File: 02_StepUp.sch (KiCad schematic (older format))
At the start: 1 part

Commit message: 3v3 über LDO von BMS enablen. Bluetooth hinzugefügt
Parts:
- removed J?: Conn_01x02_Female, symbol Connector:Conn_01x02_Female
- added C301: 1000u35V, symbol Device:CP_Small
- added C302: 1n2, symbol Device:C_Small
- added C303: 100n, symbol Device:C_Small
- added C304: 25uF, symbol Device:C_Small
- added C305: 1000u60V, symbol Device:CP_Small
- added D301: STPS2045C, symbol Device:D_Schottky_Small
- added L301: 10uH, symbol Device:L_Small
- added Q301: Q_NPN_BCE, symbol Device:Q_NPN_BCE
- added Q302: STP75NF75, symbol Device:Q_NMOS_DGS
- added R301: 5K1, symbol Device:R_Small
- added R302: 15K, symbol Device:R_Small
- added R303: 30K, symbol Device:R_Small
- added R304: 100K, symbol Device:R_Small
- added R305, R309: 1K, symbol Device:R_Small
- added R306: R010, symbol Device:R_Small
- added R307: 10K, symbol Device:R_Variable
- added R308: 2K94, symbol Device:R_Small
- added U301: L7812, symbol Regulator_Linear:L7812
- added U302: UC3843_SOIC8, Package_SO:SOIC-8_3.9x4.9mm_P1.27mm, symbol Regulator_Controller:UC3843_SOIC8
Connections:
- net labels added: FB_BOOST, GNDPWR, PACK+, POWER_32V
- wire segments 0 -> 59
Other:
- note added: "UC1842 Step Up von aliexpress yo\n\n"

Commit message: Footprintzuordnung angefangen
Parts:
- added C306: C_Small, Capacitor_SMD:C_0603_1608Metric_Pad1.05x0.95mm_HandSolder, symbol Device:C_Small
- C301: value 1000u35V -> 1000u35V EEV-FK1V102V; footprint (none) -> Capacitor_SMD:CP_Elec_16x17.5
- C302, C303: footprint (none) -> Capacitor_SMD:C_0603_1608Metric_Pad1.05x0.95mm_HandSolder
- C304: footprint (none) -> Capacitor_SMD:CP_Elec_5x5.4
- C305: value 1000u60V -> 1000u60V EEV-FK1V102V; footprint (none) -> Capacitor_SMD:CP_Elec_16x17.5
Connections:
- net labels added: POWER_AMP, SYSTEM_LOAD
- net labels removed: PACK+, POWER_32V
- wire segments 59 -> 60
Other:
- note added: "Close to VREF Pin"
- moved on the sheet: C303
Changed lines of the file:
@@
 P 7400 3600
 F 0 "C305" H 7488 3646 50  0000 L CNN
-F 1 "1000u60V" H 7488 3555 50  0000 L CNN
-F 2 "" H 7400 3600 50  0001 C CNN
+F 1 "1000u60V EEV-FK1V102V " H 6800 3500 50  0000 L CNN
+F 2 "Capacitor_SMD:CP_Elec_16x17.5" H 7400 3600 50  0001 C CNN
 F 3 "~" H 7400 3600 50  0001 C CNN
 	1    7400 3600
@@
 L Device:C_Small C303
 U 1 1 5E79837A
-P 4400 3850
-F 0 "C303" H 4492 3896 50  0000 L CNN
-F 1 "100n" H 4492 3805 50  0000 L CNN
-F 2 "" H 4400 3850 50  0001 C CNN
-F 3 "~" H 4400 3850 50  0001 C CNN
-	1    4400 3850
-	1    0    0    -1
-$EndComp
-Wire Wire Line
-	4750 3650 4400 3650
-Wire Wire Line
-	4400 3650 4400 3750
+P 4600 3850
+F 0 "C303" H 4400 3950 50  0000 L CNN
+F 1 "100n" H 4400 3750 50  0000 L CNN
+F 2 "Capacitor_SMD:C_0603_1608Metric_Pad1.05x0.95mm_HandSolder" H 4600 3850 50  0001 C CNN
+F 3 "~" H 4600 3850 50  0001 C CNN
+	1    4600 3850
+	1    0    0    -1
+$EndComp
+Wire Wire Line
+	4750 3650 4600 3650
+Wire Wire Line
+	4600 3650 4600 3750
 Wire Wire Line
 	7900 3900 8250 3900
@@
 FB_BOOST
 Wire Wire Line
-	4400 3950 4400 4150
-Wire Wire Line
-	4400 4150 4650 4150
-Wire Wire Line
-	4750 3800 4650 3800
-Wire Wire Line
-	4650 3800 4650 4150
-Connection ~ 4650 4150
-Wire Wire Line
-	4650 4150 4800 4150
+	4600 3950 4600 4150
+Wire Wire Line
+	4600 4150 4750 4150
+Wire Wire Line
+	4750 3800 4750 4150
+Connection ~ 4750 4150
+Wire Wire Line
+	4750 4150 4800 4150
 $Comp
 L power:GNDPWR #PWR0123
@@
 F 0 "C302" H 4092 3896 50  0000 L CNN
 F 1 "1n2" H 4092 3805 50  0000 L CNN
-F 2 "" H 4000 3850 50  0001 C CNN
+F 2 "Capacitor_SMD:C_0603_1608Metric_Pad1.05x0.95mm_HandSolder" H 4000 3850 50  0001 C CNN
 F 3 "~" H 4000 3850 50  0001 C CNN
 	1    4000 3850
@@
 	4000 4200 4000 3950
 Wire Wire Line
-	4750 3500 4750 3600
-Wire Wire Line
-	4750 3600 4200 3600
-Wire Wire Line
-	4200 3600 4200 3700
-Wire Wire Line
-	4200 3700 4000 3700
+	4450 3700 4000 3700
 Connection ~ 4000 3700
 Wire Wire Line
@@
 Connection ~ 6050 2600
 Text GLabel 3900 2600 0    50   Input ~ 0
-PACK+
+SYSTEM_LOAD
 $Comp
 L Regulator_Linear:L7812 U301
@@
 P 3950 3000
 F 0 "C301" H 4038 3046 50  0000 L CNN
-F 1 "1000u35V" H 4038 2955 50  0000 L CNN
-F 2 "" H 3950 3000 50  0001 C CNN
+F 1 "1000u35V EEV-FK1V102V " H 3400 2900 50  0000 L CNN
+F 2 "Capacitor_SMD:CP_Elec_16x17.5" H 3950 3000 50  0001 C CNN
 F 3 "~" H 3950 3000 50  0001 C CNN
 	1    3950 3000
@@
 F 0 "C304" H 4992 3046 50  0000 L CNN
 F 1 "25uF" H 4992 2955 50  0000 L CNN
-F 2 "" H 4900 3000 50  0001 C CNN
+F 2 "Capacitor_SMD:CP_Elec_5x5.4" H 4900 3000 50  0001 C CNN
 F 3 "~" H 4900 3000 50  0001 C CNN
 	1    4900 3000
@@
 	5900 4200 5900 3700
 Text GLabel 8250 3150 2    50   Output ~ 0
-POWER_32V
+POWER_AMP
+$Comp
+L Device:C_Small C306
+U 1 1 5EB77D85
+P 2800 3850
+F 0 "C306" H 2892 3896 50  0000 L CNN
+F 1 "C_Small" H 2892 3805 50  0000 L CNN
+F 2 "Capacitor_SMD:C_0603_1608Metric_Pad1.05x0.95mm_HandSolder" H 2800 3850 50  0001 C CNN
+F 3 "~" H 2800 3850 50  0001 C CNN
+	1    2800 3850
+	1    0    0    -1
+$EndComp
+Wire Wire Line
+	4750 3500 4450 3500
+Wire Wire Line
+	4450 3500 4450 3700
+Wire Wire Line
+	3600 3400 2800 3400
+Wire Wire Line
+	2800 3400 2800 3750
+Connection ~ 3600 3400
+$Comp
+L power:GNDPWR #PWR0178
+U 1 1 5EB800AE
+P 2800 4100
+F 0 "#PWR0178" H 2800 3900 50  0001 C CNN
+F 1 "GNDPWR" H 2804 3946 50  0000 C CNN
+F 2 "" H 2800 4050 50  0001 C CNN
+F 3 "" H 2800 4050 50  0001 C CNN
+	1    2800 4100
+	1    0    0    -1
+$EndComp
+Wire Wire Line
+	2800 3950 2800 4100
+Text Notes 2700 4100 1    50   ~ 0
+Close to VREF Pin
+$Comp
+L power:PWR_FLAG #FLG0110
+U 1 1 5EBB228F
+P 7900 3150
+F 0 "#FLG0110" H 7900 3225 50  0001 C CNN
+F 1 "PWR_FLAG" H 7900 3324 50  0000 C CNN
+F 2 "" H 7900 3150 50  0001 C CNN
+F 3 "~" H 7900 3150 50  0001 C CNN
+	1    7900 3150
+	1    0    0    -1
+$EndComp
 $EndSCHEMATC

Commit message: fast alle footprints herausgesucht. Spulen typen rausgesucht: Bourns spulen
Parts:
- removed D301: STPS2045C, symbol Device:D_Schottky_Small
- removed Q301: Q_NPN_BCE, symbol Device:Q_NPN_BCE
- removed Q302: STP75NF75, symbol Device:Q_NMOS_DGS
- removed R307: 10K, symbol Device:R_Variable
- added D301: STPS2045C, Package_TO_SOT_SMD:TO-263-2, symbol Device:D_Schottky_x2_KCom_AKA
- added HS301, HS302: Heatsink_Pad, Heatsink:Heatsink_AAVID_573300D00010G_TO-263, symbol Mechanical:Heatsink_Pad
- added Q301: MMBT2222LT1G, Package_TO_SOT_SMD:SOT-23, symbol Device:Q_NPN_BEC
- added Q302: TK7R7P10PL, Package_TO_SOT_SMD:TO-263-2, symbol Device:Q_NMOS_GDS
- added RV301: 10K, Potentiometer_SMD:Potentiometer_Bourns_3314J_Vertical, symbol Device:R_POT
- L301: value 10uH -> 10uH PQ2617BHA-100K; footprint (none) -> Inductor_SMD:PQ2617BHA-330K
- R301, R302, R303, R304, R305, R308, R309: footprint (none) -> Resistor_SMD:R_0603_1608Metric_Pad1.05x0.95mm_HandSolder
- R306: footprint (none) -> Resistor_SMD:R_1206_3216Metric_Pad1.42x1.75mm_HandSolder
- U301: footprint (none) -> Package_TO_SOT_SMD:TO-263-2
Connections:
- wire segments 60 -> 74
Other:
- note added: "STB75NF75"
- note added: "UC1842 Step Up von aliexpress yo\nhttps://www.360customs.de/2014/05/103050100w-led-applikation-treiber/?cookie-state-change=1586628857397\n"
- note removed: "UC1842 Step Up von aliexpress yo\n\n"
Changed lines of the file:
@@
 $EndDescr
 Text Notes 5000 1550 0    50   ~ 0
-UC1842 Step Up von aliexpress yo\n\n
+UC1842 Step Up von aliexpress yo\nhttps://www.360customs.de/2014/05/103050100w-led-applikation-treiber/?cookie-state-change=1586628857397\n
 $Comp
 L Regulator_Controller:UC3843_SOIC8 U302
@@
 F 0 "R303" H 5959 3646 50  0000 L CNN
 F 1 "30K" H 5959 3555 50  0000 L CNN
-F 2 "" H 5900 3600 50  0001 C CNN
+F 2 "Resistor_SMD:R_0603_1608Metric_Pad1.05x0.95mm_HandSolder" H 5900 3600 50  0001 C CNN
 F 3 "~" H 5900 3600 50  0001 C CNN
 	1    5900 3600
@@
 F 0 "R305" V 6104 3800 50  0000 C CNN
 F 1 "1K" V 6195 3800 50  0000 C CNN
-F 2 "" H 6300 3800 50  0001 C CNN
+F 2 "Resistor_SMD:R_0603_1608Metric_Pad1.05x0.95mm_HandSolder" H 6300 3800 50  0001 C CNN
 F 3 "~" H 6300 3800 50  0001 C CNN
 	1    6300 3800
@@
 F 0 "R306" H 6491 4054 50  0000 R CNN
 F 1 "R010" H 6491 4145 50  0000 R CNN
-F 2 "" H 6550 4100 50  0001 C CNN
+F 2 "Resistor_SMD:R_1206_3216Metric_Pad1.42x1.75mm_HandSolder" H 6550 4100 50  0001 C CNN
 F 3 "~" H 6550 4100 50  0001 C CNN
 	1    6550 4100
 	-1   0    0    1
-$EndComp
-$Comp
-L Device:Q_NMOS_DGS Q302
-U 1 1 5E7966A0
-P 6450 3400
-F 0 "Q302" H 6656 3446 50  0000 L CNN
-F 1 "STP75NF75" H 6656 3355 50  0000 L CNN
-F 2 "" H 6650 3500 50  0001 C CNN
-F 3 "~" H 6450 3400 50  0001 C CNN
-	1    6450 3400
-	1    0    0    -1
 $EndComp
 $Comp
@@
 F 0 "R304" H 5991 2854 50  0000 R CNN
 F 1 "100K" H 5991 2945 50  0000 R CNN
-F 2 "" H 6050 2900 50  0001 C CNN
+F 2 "Resistor_SMD:R_0603_1608Metric_Pad1.05x0.95mm_HandSolder" H 6050 2900 50  0001 C CNN
 F 3 "~" H 6050 2900 50  0001 C CNN
 	1    6050 2900
@@
 P 6550 2900
 F 0 "L301" H 6598 2946 50  0000 L CNN
-F 1 "10uH" H 6598 2855 50  0000 L CNN
-F 2 "" H 6550 2900 50  0001 C CNN
-F 3 "~" H 6550 2900 50  0001 C CNN
+F 1 "10uH PQ2617BHA-100K " H 6598 2855 50  0000 L CNN
+F 2 "Inductor_SMD:PQ2617BHA-330K" H 6550 2900 50  0001 C CNN
+F 3 "https://www.mouser.de/datasheet/2/54/bourns_PQ2617BHA_datasheet-1159314.pdf" H 6550 2900 50  0001 C CNN
 	1    6550 2900
 	1    0    0    -1
@@
 Wire Wire Line
 	6550 3000 6550 3150
-$Comp
-L Device:D_Schottky_Small D301
-U 1 1 5E796C90
-P 7250 3150
-F 0 "D301" H 7250 2945 50  0000 C CNN
-F 1 "STPS2045C" H 7250 3036 50  0000 C CNN
-F 2 "" V 7250 3150 50  0001 C CNN
-F 3 "~" V 7250 3150 50  0001 C CNN
-	1    7250 3150
-	-1   0    0    1
-$EndComp
-Wire Wire Line
-	7150 3150 6550 3150
 Connection ~ 6550 3150
 Wire Wire Line
@@
 	7400 4200 7400 3700
 $Comp
-L Device:R_Variable R307
-U 1 1 5E79725B
-P 7900 3400
-F 0 "R307" H 8028 3446 50  0000 L CNN
-F 1 "10K" H 8028 3355 50  0000 L CNN
-F 2 "" V 7830 3400 50  0001 C CNN
-F 3 "~" H 7900 3400 50  0001 C CNN
-	1    7900 3400
-	1    0    0    -1
-$EndComp
-$Comp
 L Device:R_Small R308
 U 1 1 5E7975A3
@@
 F 0 "R308" H 7841 3704 50  0000 R CNN
 F 1 "2K94" H 7841 3795 50  0000 R CNN
-F 2 "" H 7900 3750 50  0001 C CNN
+F 2 "Resistor_SMD:R_0603_1608Metric_Pad1.05x0.95mm_HandSolder" H 7900 3750 50  0001 C CNN
 F 3 "~" H 7900 3750 50  0001 C CNN
 	1    7900 3750
@@
 F 0 "R309" H 7841 4004 50  0000 R CNN
 F 1 "1K" H 7841 4095 50  0000 R CNN
-F 2 "" H 7900 4050 50  0001 C CNN
+F 2 "Resistor_SMD:R_0603_1608Metric_Pad1.05x0.95mm_HandSolder" H 7900 4050 50  0001 C CNN
 F 3 "~" H 7900 4050 50  0001 C CNN
 	1    7900 4050
@@
 	7900 3950 7900 3900
 Wire Wire Line
-	7900 3650 7900 3550
+	7900 3650 7900 3600
 $Comp
 L power:GNDPWR #PWR0122
@@
 	7900 3250 7900 3150
 Wire Wire Line
-	7900 3150 7400 3150
+	7900 3150 7600 3150
 Connection ~ 7400 3150
 Wire Wire Line
@@
 Wire Wire Line
 	4600 3650 4600 3750
-Wire Wire Line
-	7900 3900 8250 3900
 Connection ~ 7900 3900
 Wire Wire Line
 	7900 3900 7900 3850
-Text Label 8250 3900 0    50   ~ 0
-FB_BOOST
-Text Label 4800 4150 0    50   ~ 0
+Text Label 6500 4600 0    50   ~ 0
 FB_BOOST
 Wire Wire Line
@@
 	4750 3800 4750 4150
 Connection ~ 4750 4150
-Wire Wire Line
-	4750 4150 4800 4150
 $Comp
 L power:GNDPWR #PWR0123
@@
 F 0 "R302" H 4059 3546 50  0000 L CNN
 F 1 "15K" H 4059 3455 50  0000 L CNN
-F 2 "" H 4000 3500 50  0001 C CNN
+F 2 "Resistor_SMD:R_0603_1608Metric_Pad1.05x0.95mm_HandSolder" H 4000 3500 50  0001 C CNN
 F 3 "~" H 4000 3500 50  0001 C CNN
 	1    4000 3500
@@
 Wire Wire Line
 	4000 3700 4000 3750
-$Comp
-L Device:Q_NPN_BCE Q301
-U 1 1 5E79D498
-P 3700 3700
-F 0 "Q301" H 3890 3746 50  0000 L CNN
-F 1 "Q_NPN_BCE" H 3890 3655 50  0000 L CNN
-F 2 "" H 3900 3800 50  0001 C CNN
-F 3 "~" H 3700 3700 50  0001 C CNN
-	1    3700 3700
-	-1   0    0    -1
-$EndComp
 Wire Wire Line
 	4000 3700 3900 3700
@@
 F 0 "R301" H 3659 4146 50  0000 L CNN
 F 1 "5K1" H 3659 4055 50  0000 L CNN
-F 2 "" H 3600 4100 50  0001 C CNN
+F 2 "Resistor_SMD:R_0603_1608Metric_Pad1.05x0.95mm_HandSolder" H 3600 4100 50  0001 C CNN
 F 3 "~" H 3600 4100 50  0001 C CNN
 	1    3600 4100
@@
 F 0 "U301" H 4550 3042 50  0000 C CNN
 F 1 "L7812" H 4550 2951 50  0000 C CNN
-F 2 "" H 4575 2650 50  0001 L CIN
+F 2 "Package_TO_SOT_SMD:TO-263-2" H 4575 2650 50  0001 L CIN
 F 3 "http://www.st.com/content/ccc/resource/technical/document/datasheet/41/4f/b3/b0/12/d4/47/88/CD00000444.pdf/files/CD00000444.pdf/jcr:content/translations/en.CD00000444.pdf" H 4550 2750 50  0001 C CNN
 	1    4550 2800
@@
 	1    0    0    -1
 $EndComp
+$Comp
+L Mechanical:Heatsink_Pad HS301
+U 1 1 5EC9B13F
+P 7600 2700
+F 0 "HS301" H 7741 2741 50  0000 L CNN
+F 1 "Heatsink_Pad" H 7741 2650 50  0000 L CNN
+F 2 "Heatsink:Heatsink_AAVID_573300D00010G_TO-263" H 7612 2650 50  0001 C CNN
+F 3 "~" H 7612 2650 50  0001 C CNN
+	1    7600 2700
+	1    0    0    -1
+$EndComp
+Wire Wire Line
+	7600 2800 7600 3150
+Connection ~ 7600 3150
+Wire Wire Line
+	7600 3150 7400 3150
+$Comp
+L Device:Q_NMOS_GDS Q302
+U 1 1 5E929C35
+P 6450 3400
+F 0 "Q302" H 6750 3400 50  0000 L CNN
+F 1 "TK7R7P10PL" V 6700 3150 50  0000 L CNN
+F 2 "Package_TO_SOT_SMD:TO-263-2" H 6650 3500 50  0001 C CNN
+F 3 "https://www.mouser.de/datasheet/2/408/TK7R7P10PL_datasheet_en_20180219-1568652.pdf" H 6450 3400 50  0001 C CNN
+	1    6450 3400
+	1    0    0    -1
+$EndComp
+$Comp
+L Mechanical:Heatsink_Pad HS302
+U 1 1 5E929E76
+P 6400 2450
+F 0 "HS302" H 6541 2491 50  0000 L CNN
+F 1 "Heatsink_Pad" H 6541 2400 50  0000 L CNN
+F 2 "Heatsink:Heatsink_AAVID_573300D00010G_TO-263" H 6412 2400 50  0001 C CNN
+F 3 "~" H 6412 2400 50  0001 C CNN
+	1    6400 2450
+	1    0    0    -1
+$EndComp
+Wire Wire Line
+	6400 2550 6400 3150
+Wire Wire Line
+	6400 3150 6550 3150
+Text Notes 6750 3600 0    50   ~ 0
+STB75NF75
+$Comp
+L Device:D_Schottky_x2_KCom_AKA D301
+U 1 1 5EED4F08
+P 7150 3150
+F 0 "D301" V 7650 3050 50  0000 L CNN
+F 1 "STPS2045C" V 7550 3000 50  0000 L CNN
+F 2 "Package_TO_SOT_SMD:TO-263-2" H 7150 3150 50  0001 C CNN
+F 3 "https://www.mouser.de/datasheet/2/389/cd00268203-1797199.pdf" H 7150 3150 50  0001 C CNN
+	1    7150 3150
+	0    -1   -1   0
+$EndComp
+Wire Wire Line
+	7150 3450 7050 3450
+Wire Wire Line
+	7050 3450 7050 3150
+Wire Wire Line
+	7050 2850 7150 2850
+Wire Wire Line
+	6550 3150 7050 3150
+Connection ~ 7050 3150
+Wire Wire Line
+	7050 3150 7050 2850
+Wire Wire Line
+	4750 4150 4750 4600
+Wire Wire Line
+	4750 4600 7650 4600
+Wire Wire Line
+	7650 4600 7650 3900
+Wire Wire Line
+	7650 3900 7900 3900
+$Comp
+L Device:Q_NPN_BEC Q301
+U 1 1 5EEE6C27
+P 3700 3700
+F 0 "Q301" H 3890 3746 50  0000 L CNN
+F 1 "MMBT2222LT1G" H 3890 3655 50  0000 L CNN
+F 2 "Package_TO_SOT_SMD:SOT-23" H 3900 3800 50  0001 C CNN
+F 3 "https://www.mouser.de/datasheet/2/308/MMBT2222LT1-D-1811600.pdf" H 3700 3700 50  0001 C CNN
+	1    3700 3700
+	-1   0    0    -1
+$EndComp
+$Comp
+L Device:R_POT RV301
+U 1 1 5EEEB2DA
+P 7900 3400
+F 0 "RV301" H 7830 3446 50  0000 R CNN
+F 1 "10K" H 7830 3355 50  0000 R CNN
+F 2 "Potentiometer_SMD:Potentiometer_Bourns_3314J_Vertical" H 7900 3400 50  0001 C CNN
+F 3 "https://www.mouser.de/datasheet/2/54/tc33-778219.pdf" H 7900 3400 50  0001 C CNN
+	1    7900 3400
+	1    0    0    -1
+$EndComp
+Wire Wire Line
+	8050 3400 8100 3400
+Wire Wire Line
+	8100 3400 8100 3600
+Wire Wire Line
+	8100 3600 7900 3600
+Connection ~ 7900 3600
+Wire Wire Line
+	7900 3600 7900 3550
 $EndSCHEMATC

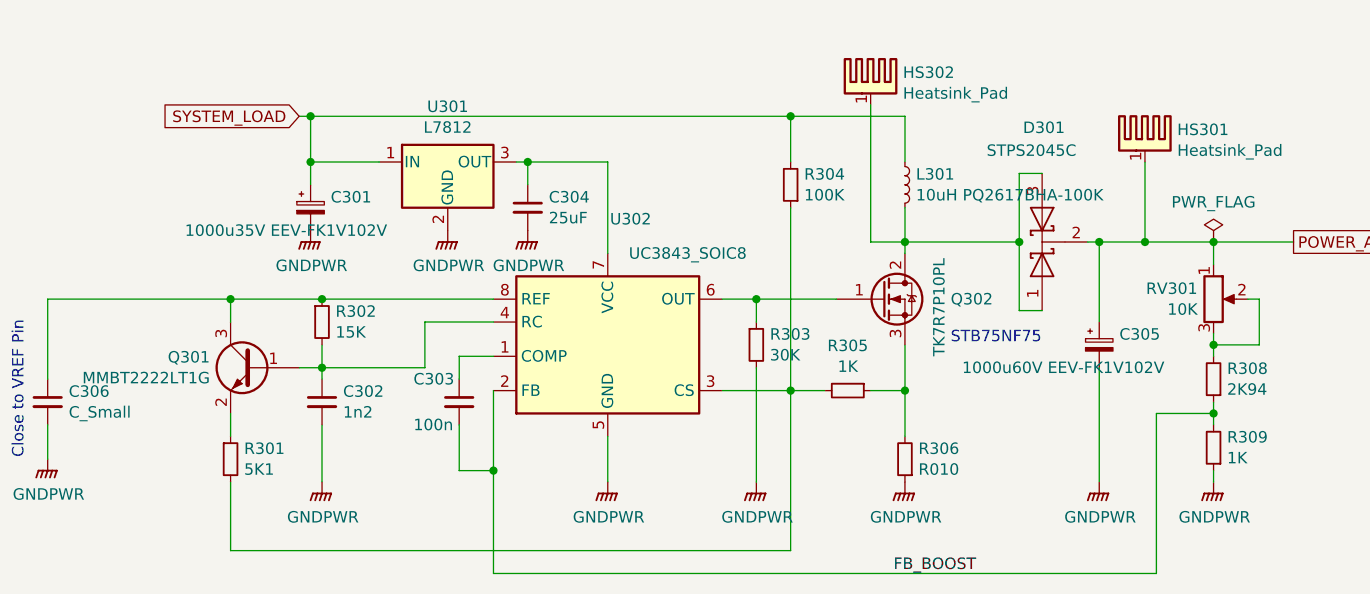
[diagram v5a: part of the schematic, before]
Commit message: Alle Parts geplaced: Dimension der Platine 200x105qmm. TODO Anzeige überarbeiten
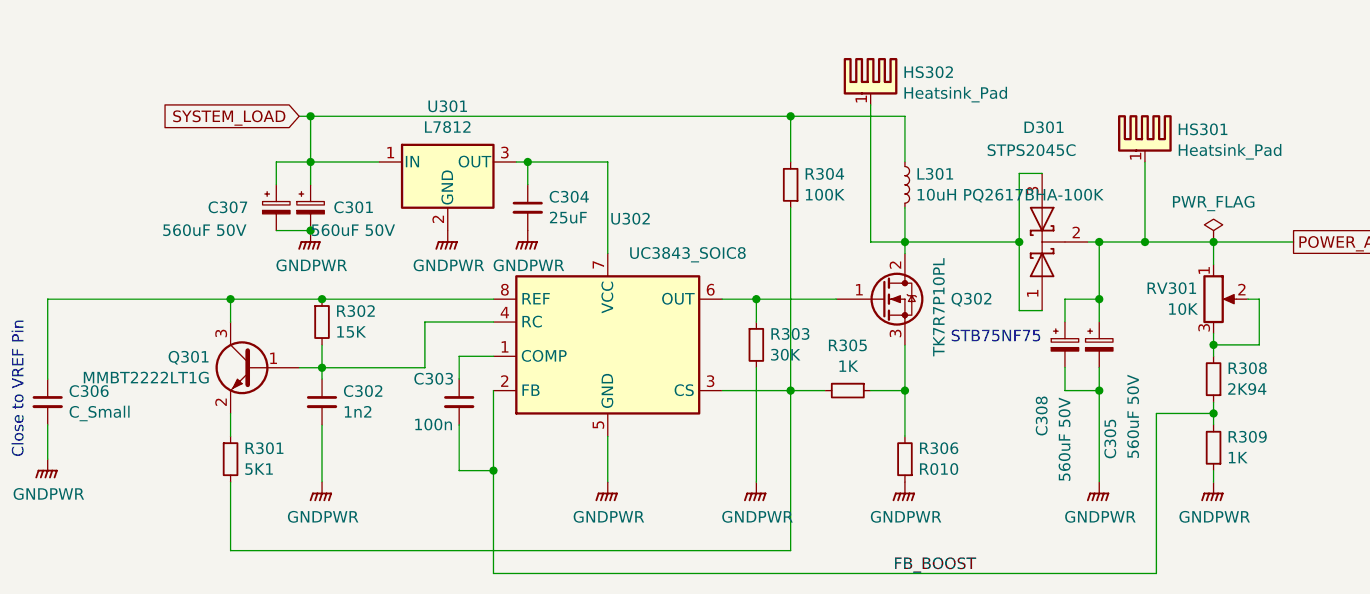
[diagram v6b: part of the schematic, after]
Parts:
- added C307, C308: 560uF 50V, Capacitor_THT:CP_Radial_D12.5mm_P5.00mm, symbol Device:CP_Small
- C301: value 1000u35V EEV-FK1V102V -> 560uF 50V; footprint Capacitor_SMD:CP_Elec_16x17.5 -> Capacitor_THT:CP_Radial_D12.5mm_P5.00mm
- C305: value 1000u60V EEV-FK1V102V -> 560uF 50V; footprint Capacitor_SMD:CP_Elec_16x17.5 -> Capacitor_THT:CP_Radial_D12.5mm_P5.00mm
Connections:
- net GNDPWR: now also C307.2, C308.2
- net POWER_AMP: now also C308.1
- net SYSTEM_LOAD: now also C307.1
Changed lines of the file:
@@
 Wire Wire Line
 	6550 3150 6550 3200
-$Comp
-L Device:CP_Small C305
-U 1 1 5E796E0D
-P 7400 3600
-F 0 "C305" H 7488 3646 50  0000 L CNN
-F 1 "1000u60V EEV-FK1V102V " H 6800 3500 50  0000 L CNN
-F 2 "Capacitor_SMD:CP_Elec_16x17.5" H 7400 3600 50  0001 C CNN
-F 3 "~" H 7400 3600 50  0001 C CNN
-	1    7400 3600
-	1    0    0    -1
-$EndComp
-Wire Wire Line
-	7400 3500 7400 3150
+Wire Wire Line
+	7400 3500 7400 3400
 Wire Wire Line
 	7400 3150 7350 3150
@@
 $EndComp
 Wire Wire Line
-	7400 4200 7400 3700
+	7400 4200 7400 3800
 $Comp
 L Device:R_Small R308
@@
 	1    0    0    -1
 $EndComp
-$Comp
-L Device:CP_Small C301
-U 1 1 5E7AB87B
-P 3950 3000
-F 0 "C301" H 4038 3046 50  0000 L CNN
-F 1 "1000u35V EEV-FK1V102V " H 3400 2900 50  0000 L CNN
-F 2 "Capacitor_SMD:CP_Elec_16x17.5" H 3950 3000 50  0001 C CNN
-F 3 "~" H 3950 3000 50  0001 C CNN
-	1    3950 3000
-	1    0    0    -1
-$EndComp
 Wire Wire Line
 	3950 2900 3950 2800
@@
 Wire Wire Line
 	7900 3600 7900 3550
+$Comp
+L Device:CP_Small C?
+U 1 1 5E9C5E68
+P 7400 3600
+AR Path="/5E751A81/5E9C5E68" Ref="C?"  Part="1"
+AR Path="/5E73BAE8/5E9C5E68" Ref="C305"  Part="1"
+F 0 "C305" V 7450 3100 50  0000 L CNN
+F 1 "560uF 50V" V 7550 3100 50  0000 L CNN
+F 2 "Capacitor_THT:CP_Radial_D12.5mm_P5.00mm" H 7400 3600 50  0001 C CNN
+F 3 "https://www.mouser.de/datasheet/2/420/United-Chemi-Con-1109128.pdf" H 7400 3600 50  0001 C CNN
+	1    7400 3600
+	1    0    0    -1
+$EndComp
+$Comp
+L Device:CP_Small C?
+U 1 1 5E9C790D
+P 7250 3600
+AR Path="/5E751A81/5E9C790D" Ref="C?"  Part="1"
+AR Path="/5E73BAE8/5E9C790D" Ref="C308"  Part="1"
+F 0 "C308" V 7150 3200 50  0000 L CNN
+F 1 "560uF 50V" V 7250 3000 50  0000 L CNN
+F 2 "Capacitor_THT:CP_Radial_D12.5mm_P5.00mm" H 7250 3600 50  0001 C CNN
+F 3 "https://www.mouser.de/datasheet/2/420/United-Chemi-Con-1109128.pdf" H 7250 3600 50  0001 C CNN
+	1    7250 3600
+	1    0    0    -1
+$EndComp
+Wire Wire Line
+	7250 3700 7250 3800
+Wire Wire Line
+	7250 3800 7400 3800
+Connection ~ 7400 3800
+Wire Wire Line
+	7400 3800 7400 3700
+Wire Wire Line
+	7250 3500 7250 3400
+Wire Wire Line
+	7250 3400 7400 3400
+Connection ~ 7400 3400
+Wire Wire Line
+	7400 3400 7400 3150
+$Comp
+L Device:CP_Small C?
+U 1 1 5E9CBBA9
+P 3950 3000
+AR Path="/5E751A81/5E9CBBA9" Ref="C?"  Part="1"
+AR Path="/5E73BAE8/5E9CBBA9" Ref="C301"  Part="1"
+F 0 "C301" H 4050 3000 50  0000 L CNN
+F 1 "560uF 50V" H 3950 2900 50  0000 L CNN
+F 2 "Capacitor_THT:CP_Radial_D12.5mm_P5.00mm" H 3950 3000 50  0001 C CNN
+F 3 "https://www.mouser.de/datasheet/2/420/United-Chemi-Con-1109128.pdf" H 3950 3000 50  0001 C CNN
+	1    3950 3000
+	1    0    0    -1
+$EndComp
+$Comp
+L Device:CP_Small C?
+U 1 1 5E9CD890
+P 3800 3000
+AR Path="/5E751A81/5E9CD890" Ref="C?"  Part="1"
+AR Path="/5E73BAE8/5E9CD890" Ref="C307"  Part="1"
+F 0 "C307" H 3500 3000 50  0000 L CNN
+F 1 "560uF 50V" H 3300 2900 50  0000 L CNN
+F 2 "Capacitor_THT:CP_Radial_D12.5mm_P5.00mm" H 3800 3000 50  0001 C CNN
+F 3 "https://www.mouser.de/datasheet/2/420/United-Chemi-Con-1109128.pdf" H 3800 3000 50  0001 C CNN
+	1    3800 3000
+	1    0    0    -1
+$EndComp
+Wire Wire Line
+	3800 2900 3800 2800
+Wire Wire Line
+	3800 2800 3950 2800
+Wire Wire Line
+	3800 3100 3950 3100
+Connection ~ 3950 3100
 $EndSCHEMATC
